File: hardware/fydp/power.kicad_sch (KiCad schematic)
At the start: 27 parts, among them J2 Conn_01x02_Pin, U59 AZ1117IH-3.3TRG1, U60 LM2611BMF/NOPB, U61 LM2733YMFX/NOPB

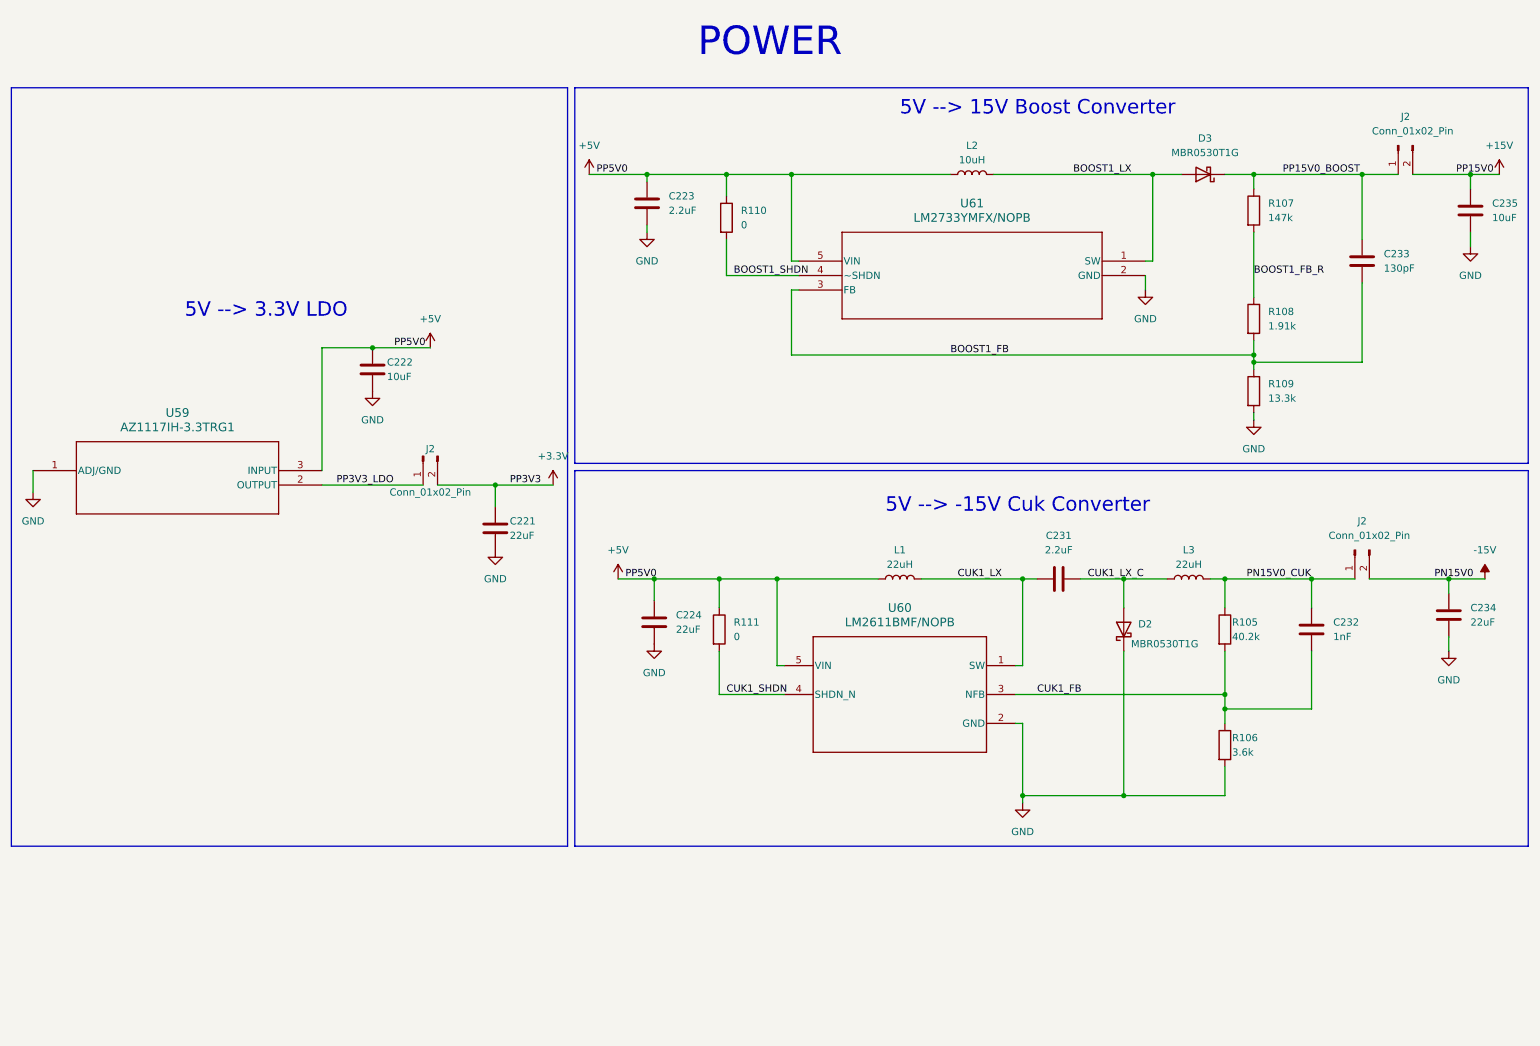
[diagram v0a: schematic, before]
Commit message: Initial layout mostly complete, need to complete lots of routing
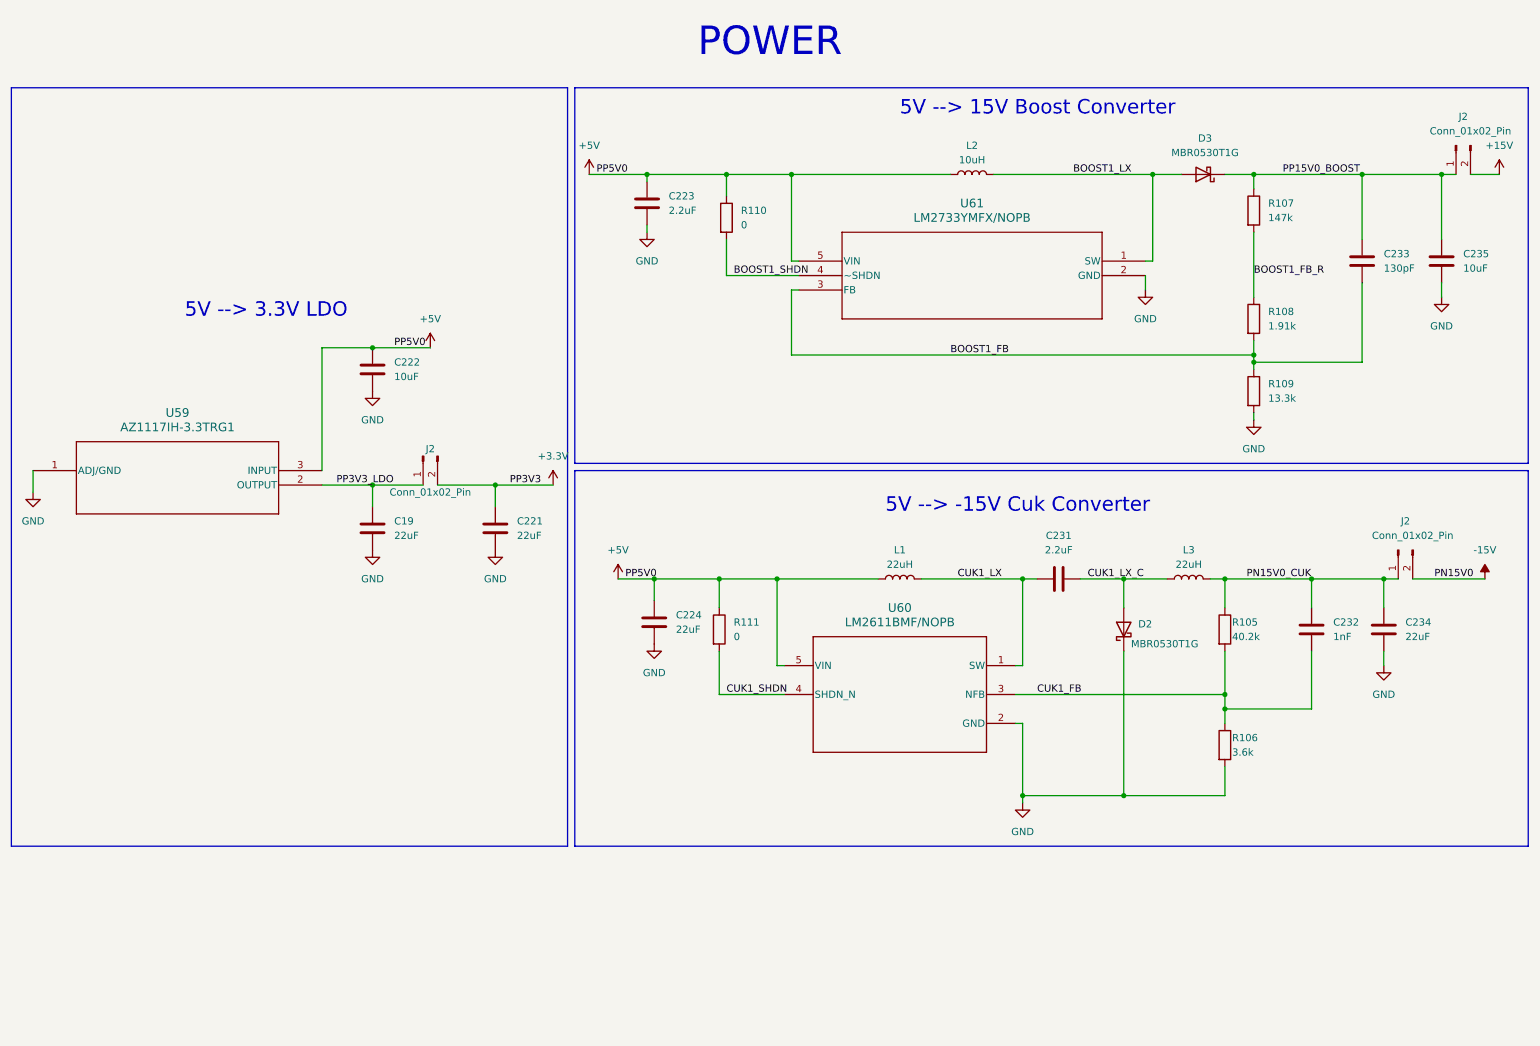
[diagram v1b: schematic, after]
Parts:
- removed J2 (x2): Conn_01x02_Pin, Connector_PinHeader_2.54mm:PinHeader_1x02_P2.54mm_Vertical, symbol Connector:Conn_01x02_Pin
- added C19: 22uF, Capacitor_SMD:C_0805_2012Metric, symbol Device:C
- added J2 (x2): Conn_01x02_Pin, Connector_PinHeader_2.54mm:PinHeader_1x02_P2.54mm_Vertical, symbol Connector:Conn_01x02_Pin
- C221, C224, C234: footprint Capacitor_SMD:C_1206_3216Metric -> Capacitor_SMD:C_0805_2012Metric; MPN CC1206MKX5R8BB226 -> CC0805MKX5R8BB226
- C222, C235: footprint Capacitor_SMD:C_1206_3216Metric -> Capacitor_SMD:C_0805_2012Metric; MPN CC1206MKX5R8BB106 -> CC0805KKX5R8BB106
- C223, C231: footprint Capacitor_SMD:C_1206_3216Metric -> Capacitor_SMD:C_0805_2012Metric; MPN CC1206JKX7R8BB225 -> CC0805KKX7R8BB225
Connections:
- net +15V: now also J2.2 (Pin_2); no longer C235.1
- net -15V: now also J2.2 (Pin_2); no longer C234.1
- net CUK1_LX: now also C231.2; no longer C231.1
- net CUK1_LX_C: now also C231.1; no longer C231.2
- net GND: now also C19.2
- net PN15V0_CUK: now also C234.1, J2.1 (Pin_1)
- net PP15V0_BOOST: now also C235.1, J2.1 (Pin_1)
- net PP3V3_LDO: now also C19.1
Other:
- moved on the sheet: C235

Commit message: Completed placement and silk for left and centre sections of the PCB
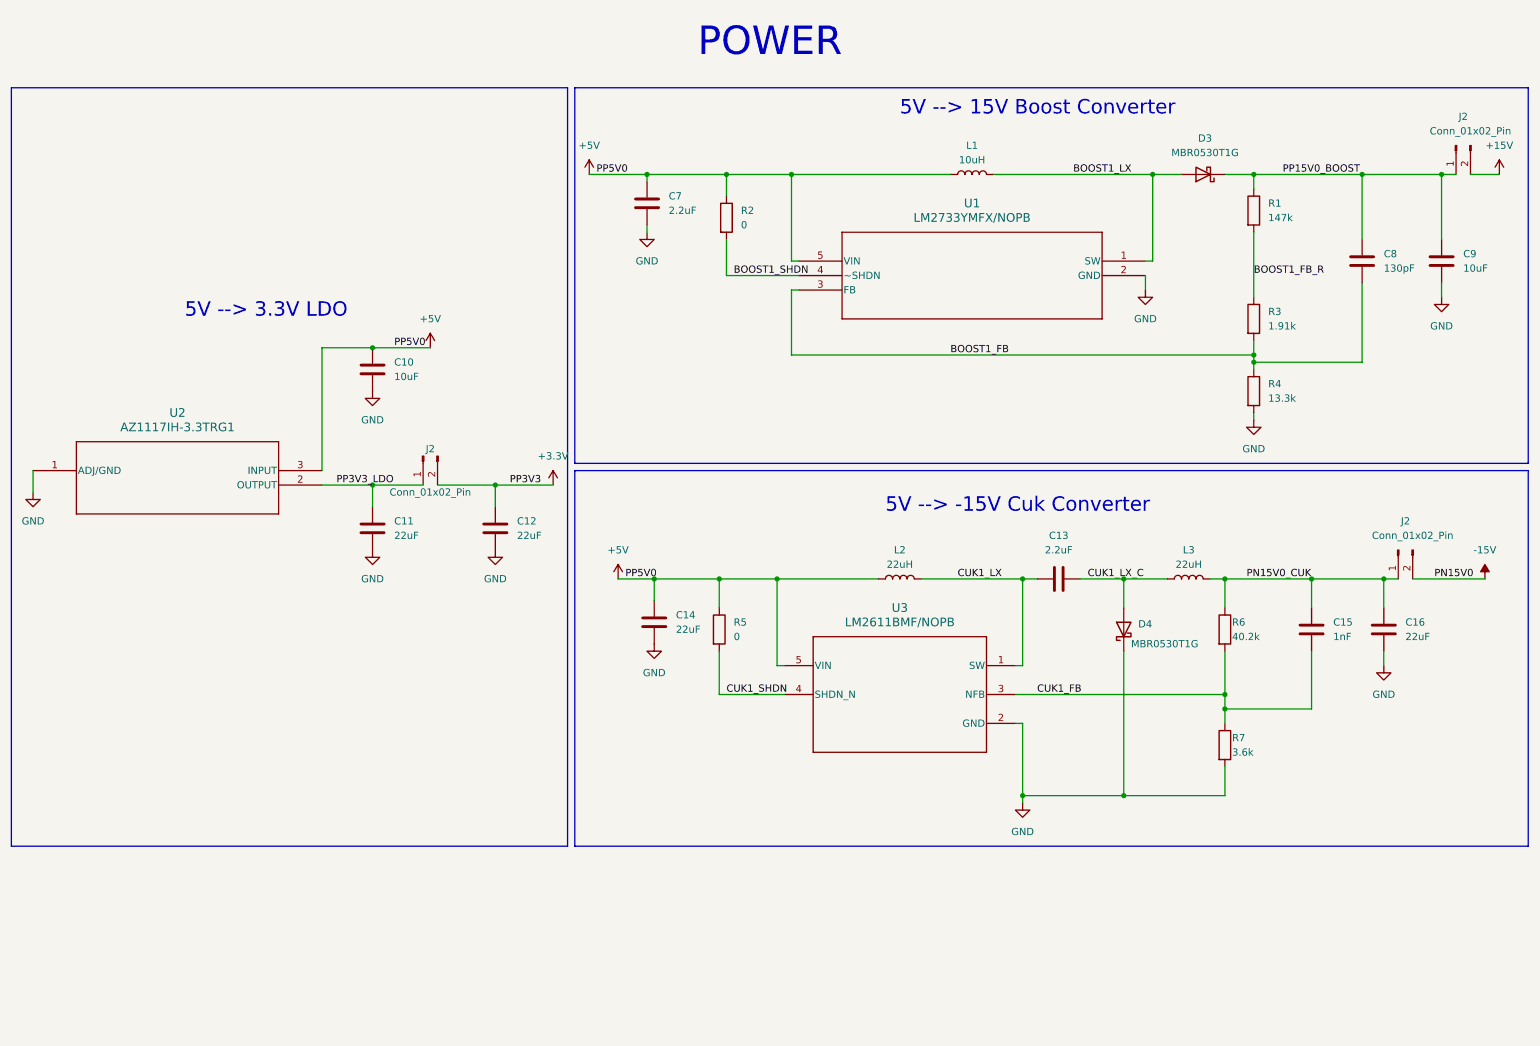
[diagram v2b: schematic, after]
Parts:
- renumbered C222 to C10, C19 to C11, C221 to C12, C231 to C13, C224 to C14, C232 to C15, C234 to C16, C223 to C7, C233 to C8, C235 to C9, D2 to D4, L2 to L1, L1 to L2, R107 to R1, R110 to R2, R108 to R3, R109 to R4, R111 to R5, R105 to R6, R106 to R7, U61 to U1, U59 to U2, U60 to U3

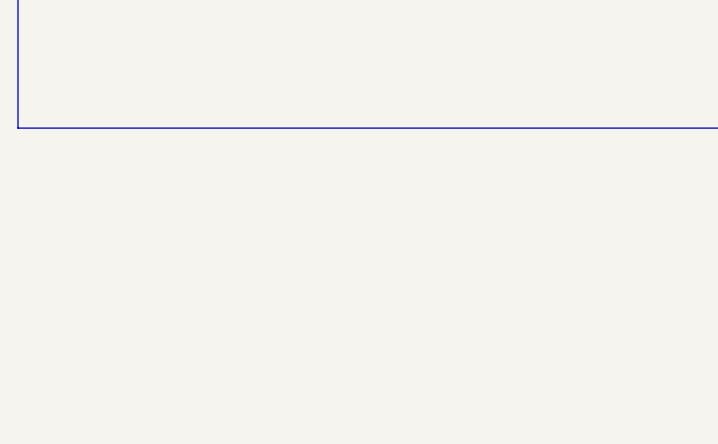
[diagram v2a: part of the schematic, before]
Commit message: Initial layout is pretty much complete, need to add power planes
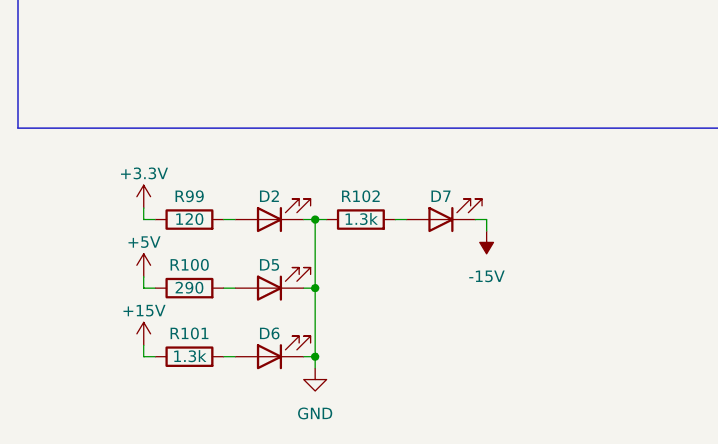
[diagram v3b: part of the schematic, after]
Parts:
- added D2, D5, D6, D7: LED, LED_SMD:LED_0805_2012Metric_Pad1.15x1.40mm_HandSolder, symbol Device:LED
- added R100: 290, Resistor_SMD:R_0805_2012Metric, symbol Device:R
- added R101, R102: 1.3k, Resistor_SMD:R_0805_2012Metric, symbol Device:R
- added R99: 120, Resistor_SMD:R_0805_2012Metric, symbol Device:R
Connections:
- net +15V: now also R101.1
- net +3.3V: now also R99.1
- net +5V: now also R100.1
- net -15V: now also D7.1 (K)
- net GND: now also D2.1 (K), D5.1 (K), D6.1 (K), R102.1
- new net: D7.2 (A), R102.2
- new net: D5.2 (A), R100.2
- new net: D2.2 (A), R99.2
- new net: D6.2 (A), R101.2

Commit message: Adding JLCPCB BOM notes
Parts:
- C10, C9: Comment (none) -> 10 µF ±10% 25V Ceramic Capacitor X5R 0805 (2012 Metric); LCSC (none) -> C89831
- C11, C12, C14, C16: Comment (none) -> 22 µF ±20% 25V Ceramic Capacitor X5R 0805 (2012 Metric); LCSC (none) -> C784585
- C13, C7: Comment (none) -> 2.2 µF ±10% 25V Ceramic Capacitor X7R 0805 (2012 Metric); LCSC (none) -> C277470
- C15: Comment (none) -> 1000 pF ±10% 50V Ceramic Capacitor X7R 0805 (2012 Metric); LCSC (none) -> C94121
- C8: Comment (none) -> 130 pF ±5% 50V Ceramic Capacitor C0G, NP0 0805 (2012 Metric); LCSC (none) -> C520003
- D2, D5, D6, D7: Comment (none) -> Green 569nm LED Indication - Discrete 2.1V 0805 (2012 Metri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; LCSC (none) -> C125090; MPN (none) -> LTST-C170GKT
- D3, D4: Comment (none) -> Diode 30 V 500mA Surface Mount SOD-123; LCSC (none) -> C82046; MPN (none) -> MBR0530T1G
- L1: Comment (none) -> 10 µH Shielded Multilayer Inductor 100 mA 390mOhm Max 0805 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; LCSC (none) -> C162582
- L2, L3: Comment (none) -> 22 µH Shielded Multilayer Inductor 220 mA 1.25Ohm 0805 (201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; LCSC (none) -> C88185; MPN LQM21DH220M70L -> MLZ2012P220WT000
- R1: Comment (none) -> 147 kOhms ±1% 0.125W, 1/8W Chip Resistor 0805 (2012 Metric)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; LCSC (none) -> C483012; MPN RT0805BRD07147KL -> RC0805FR-07147KL
- R100: Comment (none) -> 294 Ohms ±1% 0.125W, 1/8W Chip Resistor 0805 (2012 Metric) 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; LCSC (none) -> C273919
- R101, R102: Comment (none) -> 1.3 kOhms ±1% 0.125W, 1/8W Chip Resistor 0805 (2012 Metric)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; LCSC (none) -> C137582
- R2, R5: Comment (none) -> 0 Ohms Jumper Chip Resistor 0805 (2012 Metric) Moisture Res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; LCSC (none) -> C96345; MPN RC0805FR-0713K3L -> RC0805JR-070RL
- R3: Comment (none) -> 1.91 kOhms ±0.1% 0.125W, 1/8W Chip Resistor 0805 (2012 Metr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; LCSC (none) -> C865276
- R4: Comment (none) -> 13.3 kOhms ±1% 0.125W, 1/8W Chip Resistor 0805 (2012 Metric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; LCSC (none) -> C274912
- R6: Comment (none) -> 40.2 kOhms ±0.1% 0.125W, 1/8W Chip Resistor 0805 (2012 Metr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; LCSC (none) -> C865475
- R7: Comment (none) -> 3.6 kOhms ±0.1% 0.125W, 1/8W Chip Resistor 0805 (2012 Metri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; LCSC (none) -> C865466
- R99: Comment (none) -> 120 Ohms ±1% 0.125W, 1/8W Chip Resistor 0805 (2012 Metric) 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; LCSC (none) -> C114245

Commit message: Updating BOM some more
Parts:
- J2: Comment (none) -> Connector Header Through Hole 2 position 0.100" (2.54mm); MPN (none) -> TSW-102-07-G-S
- U1: Comment (none) -> Boost Switching Regulator IC Positive Adjustable 2.7V 1 Out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; LCSC (none) -> C527399; MPN (none) -> LM2733YMFX/NOPB
- U2: Comment (none) -> Linear Voltage Regulator IC Positive Fixed 1 Output 1A SOT-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; LCSC (none) -> C108495; MPN (none) -> AZ1117IH-3.3TRG1
- U3: Comment (none) -> Cuk Switching Regulator IC Negative Adjustable -1.23V 1 Out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; MPN (none) -> LM2611BMF/NOPB
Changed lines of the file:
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@@
       (effects (font (size 1.27 1.27)) hide)
     )
-    (property "Datasheet" "~" (at 259.08 111.76 0)
+    (property "Datasheet" "https://suddendocs.samtec.com/catalog_english/tsw_th.pdf" (at 259.08 111.76 0)
+      (effects (font (size 1.27 1.27)) hide)
+    )
+    (property "Comment" "Connector Header Through Hole 2 position 0.100\" (2.54mm)" (at 259.08 111.76 0)
+      (effects (font (size 1.27 1.27)) hide)
+    )
+    (property "MPN" "TSW-102-07-G-S" (at 259.08 111.76 0)
       (effects (font (size 1.27 1.27)) hide)
     )
@@
       (effects (font (size 1.27 1.27)) hide)
     )
-    (property "Datasheet" "~" (at 269.24 40.64 0)
+    (property "Datasheet" "https://suddendocs.samtec.com/catalog_english/tsw_th.pdf" (at 269.24 40.64 0)
+      (effects (font (size 1.27 1.27)) hide)
+    )
+    (property "Comment" "Connector Header Through Hole 2 position 0.100\" (2.54mm)" (at 269.24 40.64 0)
+      (effects (font (size 1.27 1.27)) hide)
+    )
+    (property "MPN" "TSW-102-07-G-S" (at 269.24 40.64 0)
       (effects (font (size 1.27 1.27)) hide)
     )
@@
       (effects (font (size 1.27 1.27)) hide)
     )
-    (property "Datasheet" "~" (at 87.63 95.25 0)
+    (property "Datasheet" "https://suddendocs.samtec.com/catalog_english/tsw_th.pdf" (at 87.63 95.25 0)
+      (effects (font (size 1.27 1.27)) hide)
+    )
+    (property "Comment" "Connector Header Through Hole 2 position 0.100\" (2.54mm)" (at 87.63 95.25 0)
+      (effects (font (size 1.27 1.27)) hide)
+    )
+    (property "MPN" "TSW-102-07-G-S" (at 87.63 95.25 0)
       (effects (font (size 1.27 1.27)) hide)
     )
@@
       (effects (font (size 1.27 1.27) italic) hide)
     )
-    (property "Datasheet" "AZ1117IH-3.3TRG1" (at 19.05 97.79 0)
+    (property "Datasheet" "https://www.diodes.com/assets/Datasheets/AZ1117I.pdf" (at 19.05 97.79 0)
       (effects (font (size 1.27 1.27) italic) hide)
+    )
+    (property "Comment" "Linear Voltage Regulator IC Positive Fixed 1 Output 1A SOT-223-3" (at 19.05 97.79 0)
+      (effects (font (size 1.27 1.27)) hide)
+    )
+    (property "LCSC" "C108495" (at 19.05 97.79 0)
+      (effects (font (size 1.27 1.27)) hide)
+    )
+    (property "MPN" "AZ1117IH-3.3TRG1" (at 19.05 97.79 0)
+      (effects (font (size 1.27 1.27)) hide)
     )
     (pin "1")
@@
       (effects (font (size 1.27 1.27) italic) hide)
     )
-    (property "Datasheet" "LM2733YMFX/NOPB" (at 214.63 60.96 0)
+    (property "Datasheet" "https://www.ti.com/general/docs/suppproductinfo.tsp?distId=10&gotoUrl=https%3A%2F%2Fwww.ti.com%2Flit%2Fgpn%2Flm2733" (at 214.63 60.96 0)
       (effects (font (size 1.27 1.27) italic) hide)
+    )
+    (property "Comment" "Boost Switching Regulator IC Positive Adjustable 2.7V 1 Output 1A (Switch) SC-74A, SOT-753" (at 214.63 60.96 0)
+      (effects (font (size 1.27 1.27)) hide)
+    )
+    (property "LCSC" "C527399" (at 214.63 60.96 0)
+      (effects (font (size 1.27 1.27)) hide)
+    )
+    (property "MPN" "LM2733YMFX/NOPB" (at 214.63 60.96 0)
+      (effects (font (size 1.27 1.27)) hide)
     )
     (pin "1")
@@
       (effects (font (size 1.27 1.27) italic) hide)
     )
-    (property "Datasheet" "LM2611BMF/NOPB" (at 171.45 137.16 0)
+    (property "Datasheet" "https://www.ti.com/general/docs/suppproductinfo.tsp?distId=10&gotoUrl=https%3A%2F%2Fwww.ti.com%2Flit%2Fgpn%2Flm2611" (at 171.45 137.16 0)
       (effects (font (size 1.27 1.27) italic) hide)
     )
-    (pin "1")
+    (property "Comment" "Cuk Switching Regulator IC Negative Adjustable -1.23V 1 Output 900mA SC-74A, SOT-753" (at 171.45 137.16 0)
+      (effects (font (size 1.27 1.27)) hide)
+    )
+    (property "MPN" "LM2611BMF/NOPB" (at 171.45 137.16 0)
+      (effects (font (size 1.27 1.27)) hide)
+    )
+    (pin "1")

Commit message: Fixed footprints
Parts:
- J2: value Conn_01x02_Pin -> TSW-102-07-G-S
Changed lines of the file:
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@@
       (effects (font (size 1.27 1.27)))
     )
-    (property "Value" "Conn_01x02_Pin" (at 261.62 109.22 90)
+    (property "Value" "TSW-102-07-G-S" (at 261.62 109.22 90)
       (effects (font (size 1.27 1.27)))
     )
@@
       (effects (font (size 1.27 1.27)))
     )
-    (property "Value" "Conn_01x02_Pin" (at 271.78 38.1 90)
+    (property "Value" "TSW-102-07-G-S" (at 271.78 38.1 90)
       (effects (font (size 1.27 1.27)))
     )
@@
       (effects (font (size 1.27 1.27)))
     )
-    (property "Value" "Conn_01x02_Pin" (at 88.9 101.6 90)
-      (effects (font (size 1.27 1.27)))
-    )
+    (property "Value" "TSW-102-07-G-S" (at 88.9 101.6 90)
+      (effects (font (size 1.27 1.27)))
+    )

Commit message: Fixed BOM
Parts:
- R7: LCSC C865466 -> C137533; MPN RT0805BRD073K6L -> RC0805FR-073K6L
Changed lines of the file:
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@@
       (effects (font (size 1.27 1.27)) hide)
     )
-    (property "MPN" "RT0805BRD073K6L" (at 228.6 146.05 0)
+    (property "MPN" "RC0805FR-073K6L" (at 228.6 146.05 0)
       (effects (font (size 1.27 1.27)) hide)
     )
@@
       (effects (font (size 1.27 1.27)) hide)
     )
-    (property "LCSC" "C865466" (at 228.6 146.05 0)
+    (property "LCSC" "C137533" (at 228.6 146.05 0)
       (effects (font (size 1.27 1.27)) hide)
     )
